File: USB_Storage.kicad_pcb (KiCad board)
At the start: 2 copper layers, 200 x 150 mm, 50 parts, among them J2 USB_A, U4 USBLC6-2SC6, U6 AP2112K-3.3, U7 KLM8G1GETF-B041, U9 USB2642/ML, Y3 24MHz

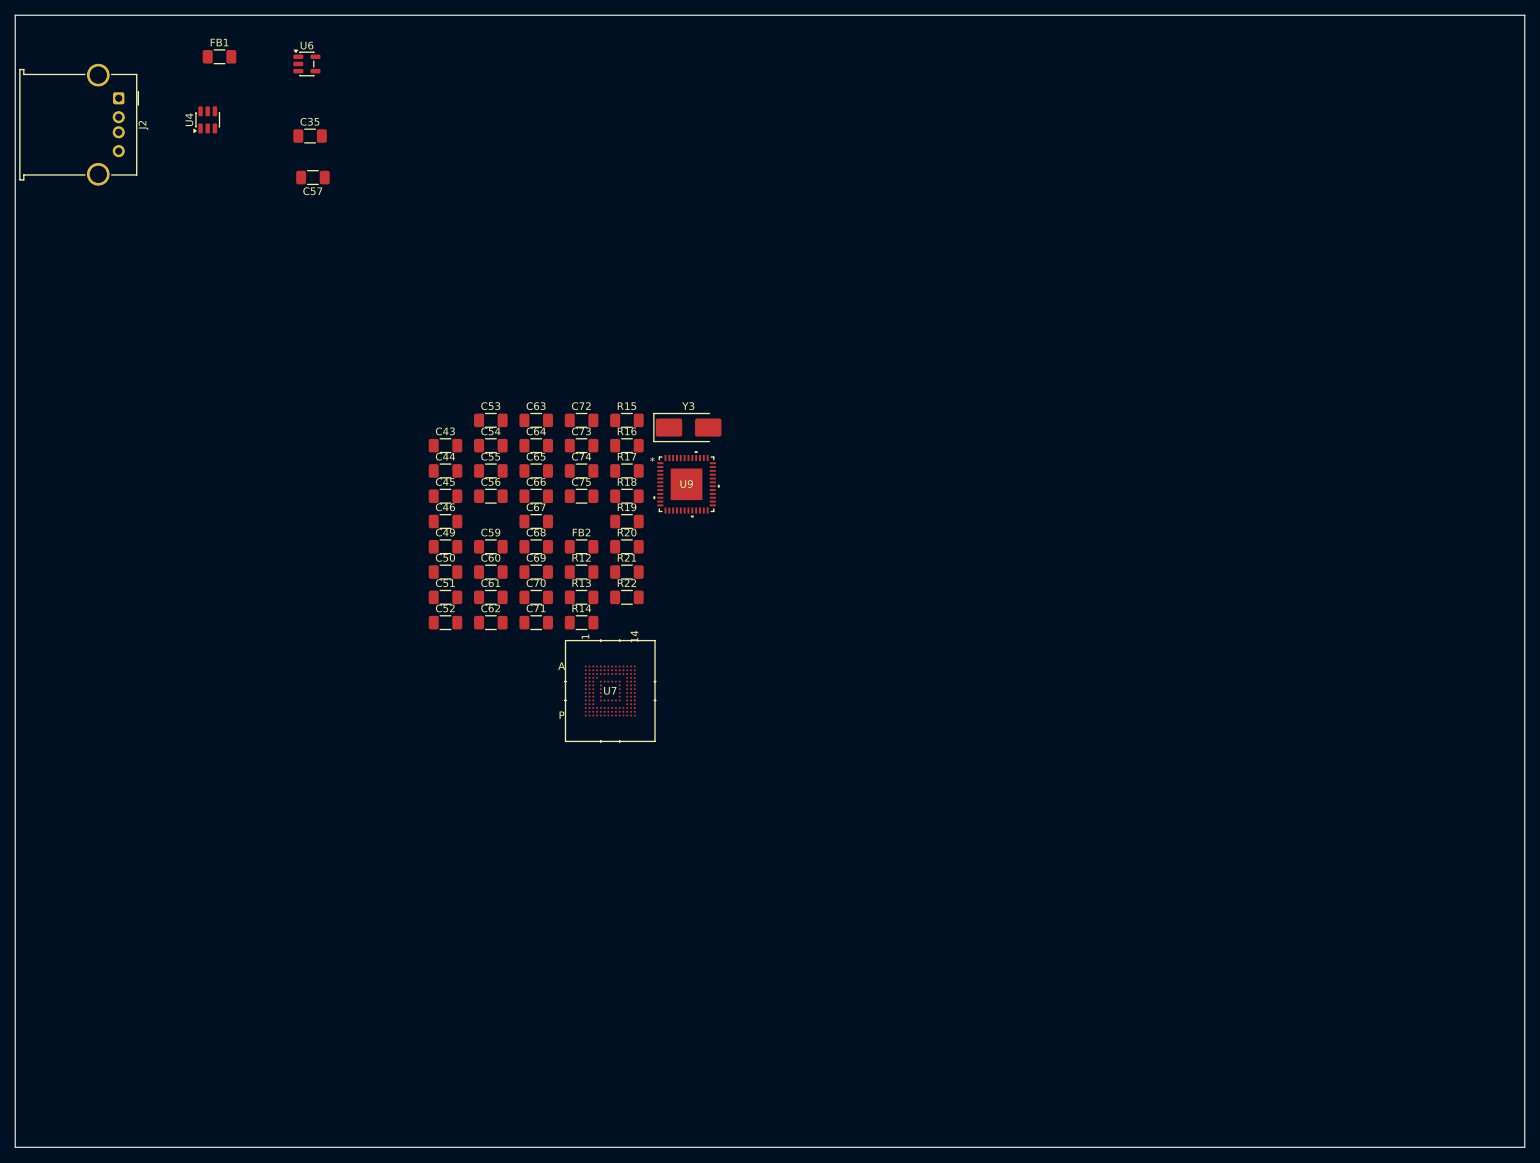
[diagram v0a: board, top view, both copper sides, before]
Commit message: PCBレイアウトの更新
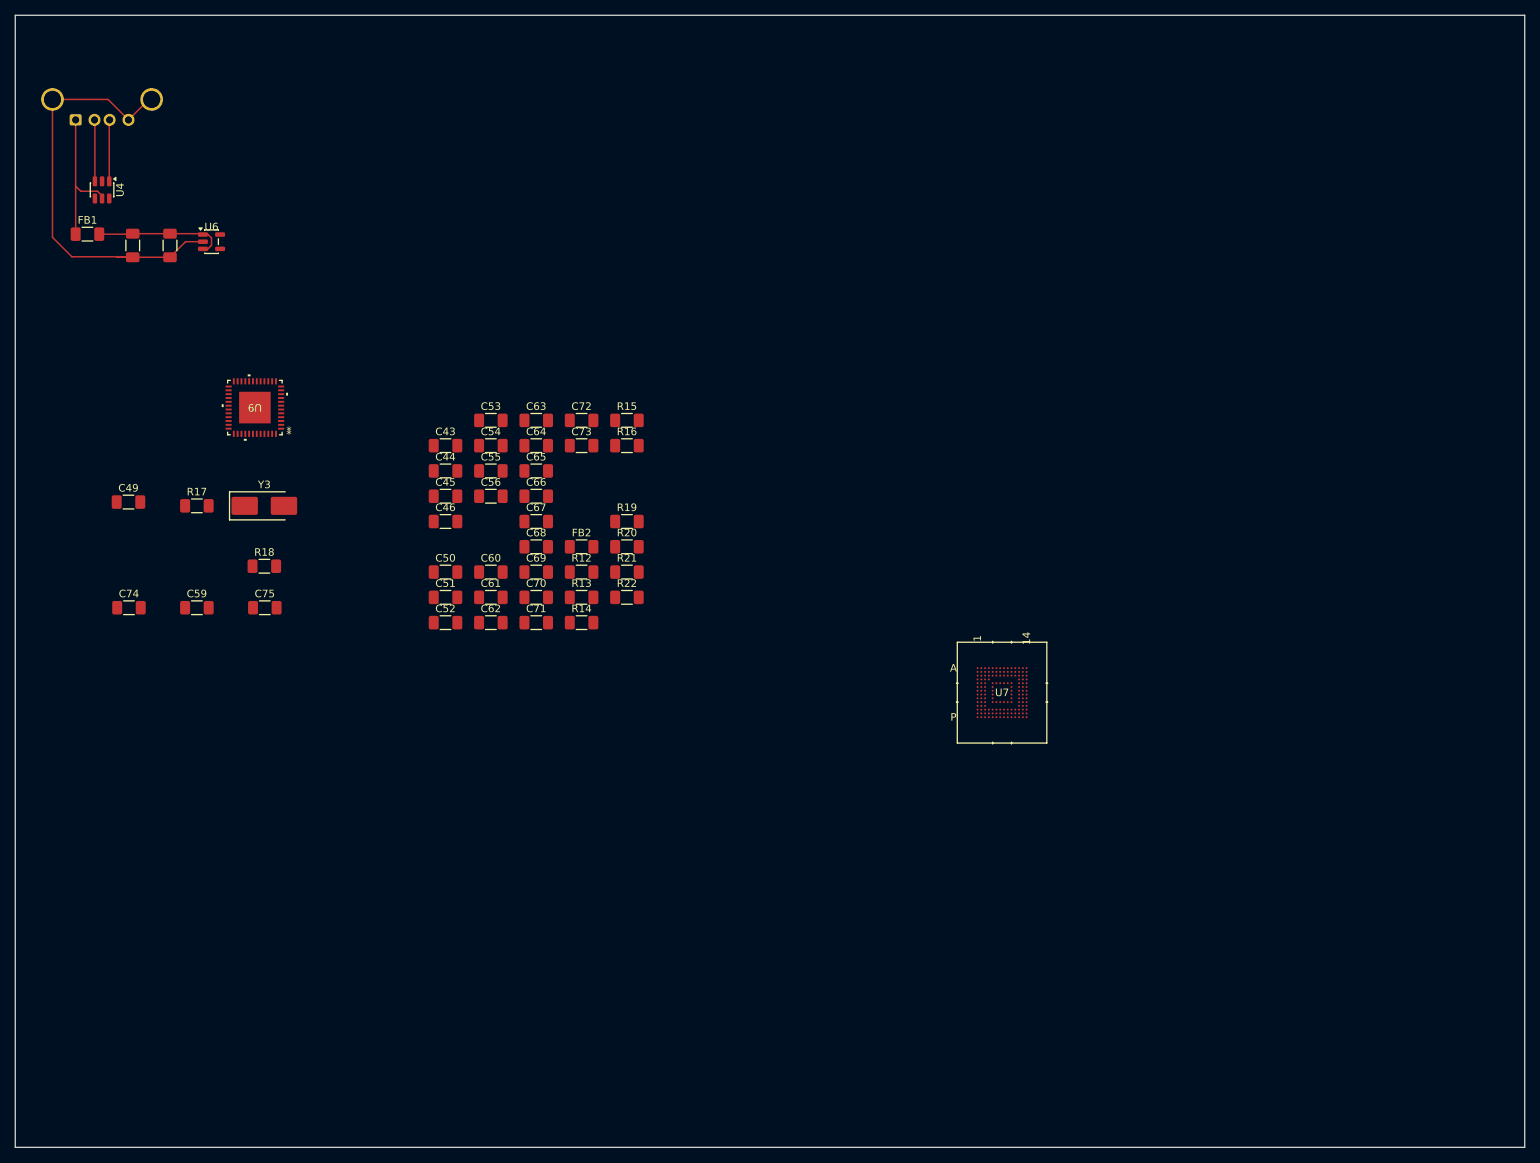
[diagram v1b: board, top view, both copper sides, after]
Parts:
- J2: moved to B.Cu
- moved C74 62.7 mm to (63.6, 93.5)
- moved U9 58.1 mm to (80.2, 67.0), turned to 180 degrees
- moved R17 57.2 mm to (72.6, 80.0)
- moved Y3 57.2 mm to (81.5, 80.0)
- moved U7 51.9 mm to (179.2, 104.8)
- moved R18 48.9 mm to (81.5, 88.0)
- moved C75 44.5 mm to (81.6, 93.5)
- moved C49 42.4 mm to (63.5, 79.5)
- moved C59 39.8 mm to (72.6, 93.5)
- moved FB1 29.3 mm to (58.1, 44.0)
- moved U6 26.7 mm to (74.5, 45.0)
- moved C57 25.5 mm to (64.1, 45.5), turned to -90 degrees
- moved C35 23.6 mm to (69.0, 45.5), turned to 90 degrees
- moved U4 16.8 mm to (60.0, 38.1), turned to -90 degrees
- moved J2 6.39 mm to (56.5, 28.9), turned to 0 degrees
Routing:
- net GND: track 0.00 -> 57.6 mm
- net /VBUS: track 0.00 -> 38.9 mm
- net /USB_DP: track 0.00 -> 8.23 mm
- net /USB_DM: track 0.00 -> 8.23 mm
